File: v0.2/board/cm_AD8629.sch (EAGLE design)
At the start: 36 parts, among them U1 LT8582EDKDPBF

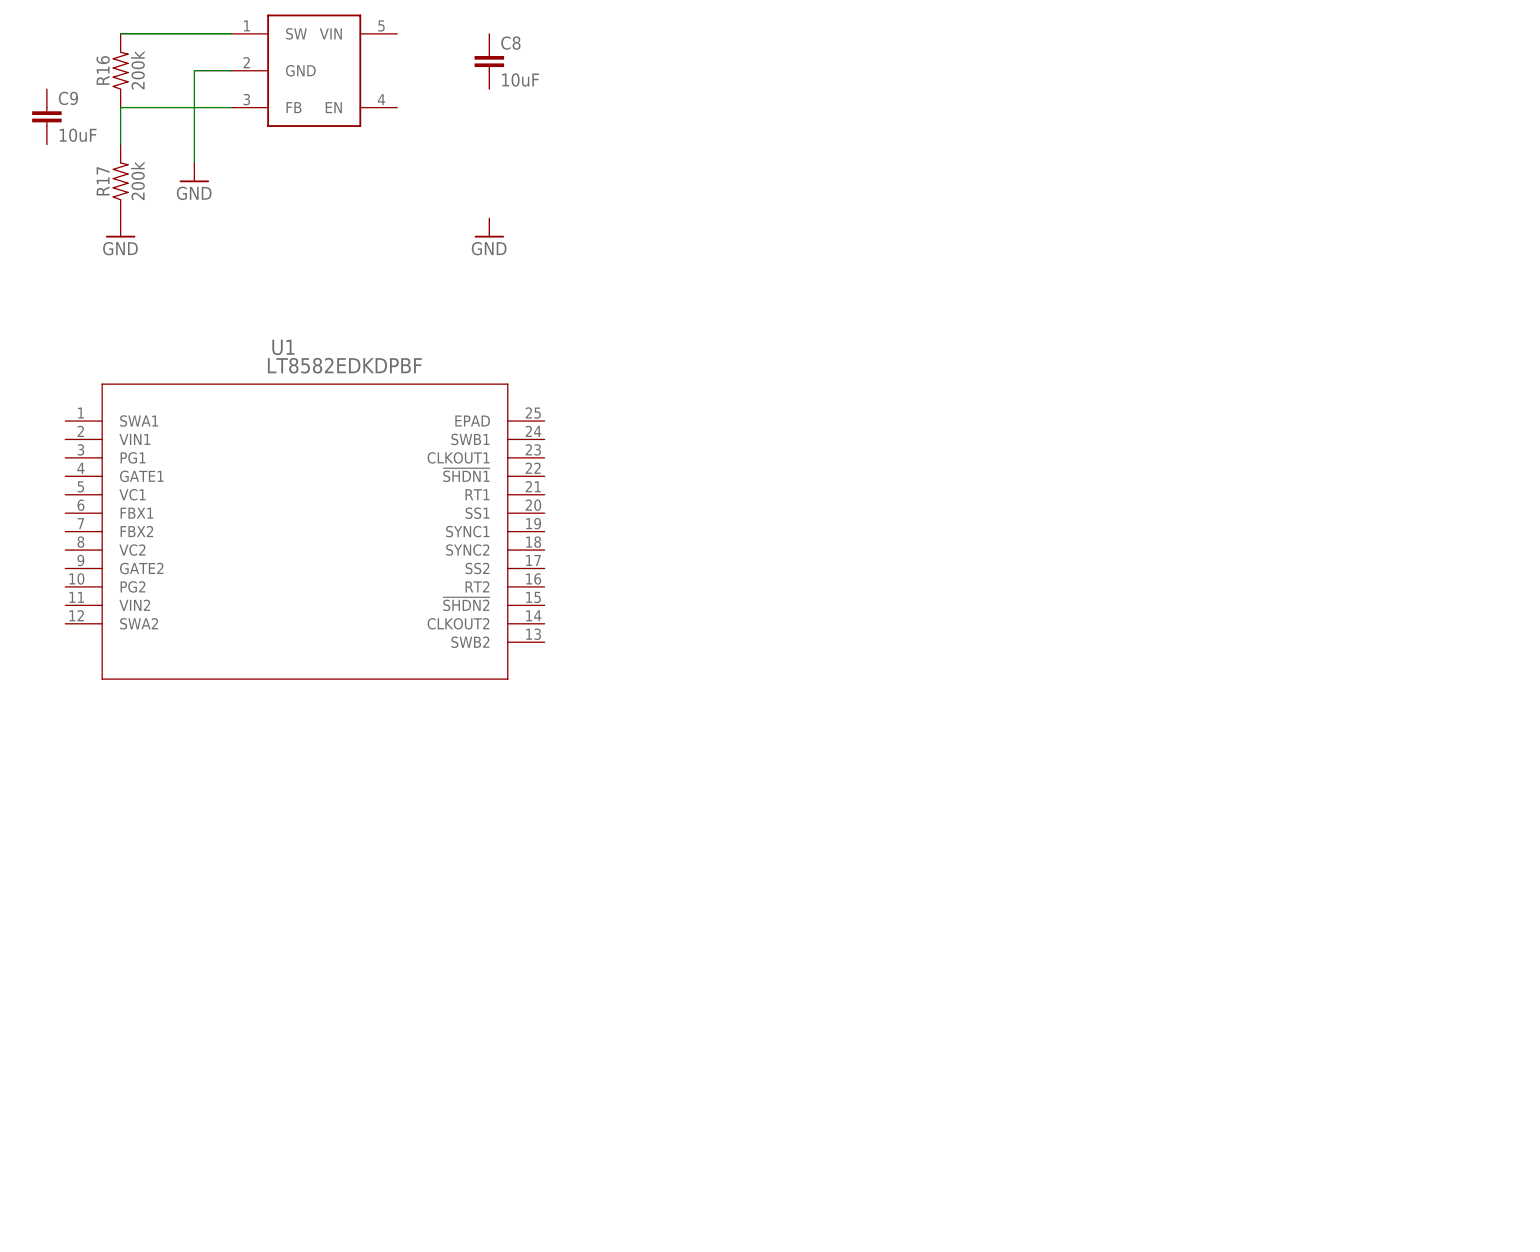
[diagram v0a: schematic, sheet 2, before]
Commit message: add 12v boost to sch
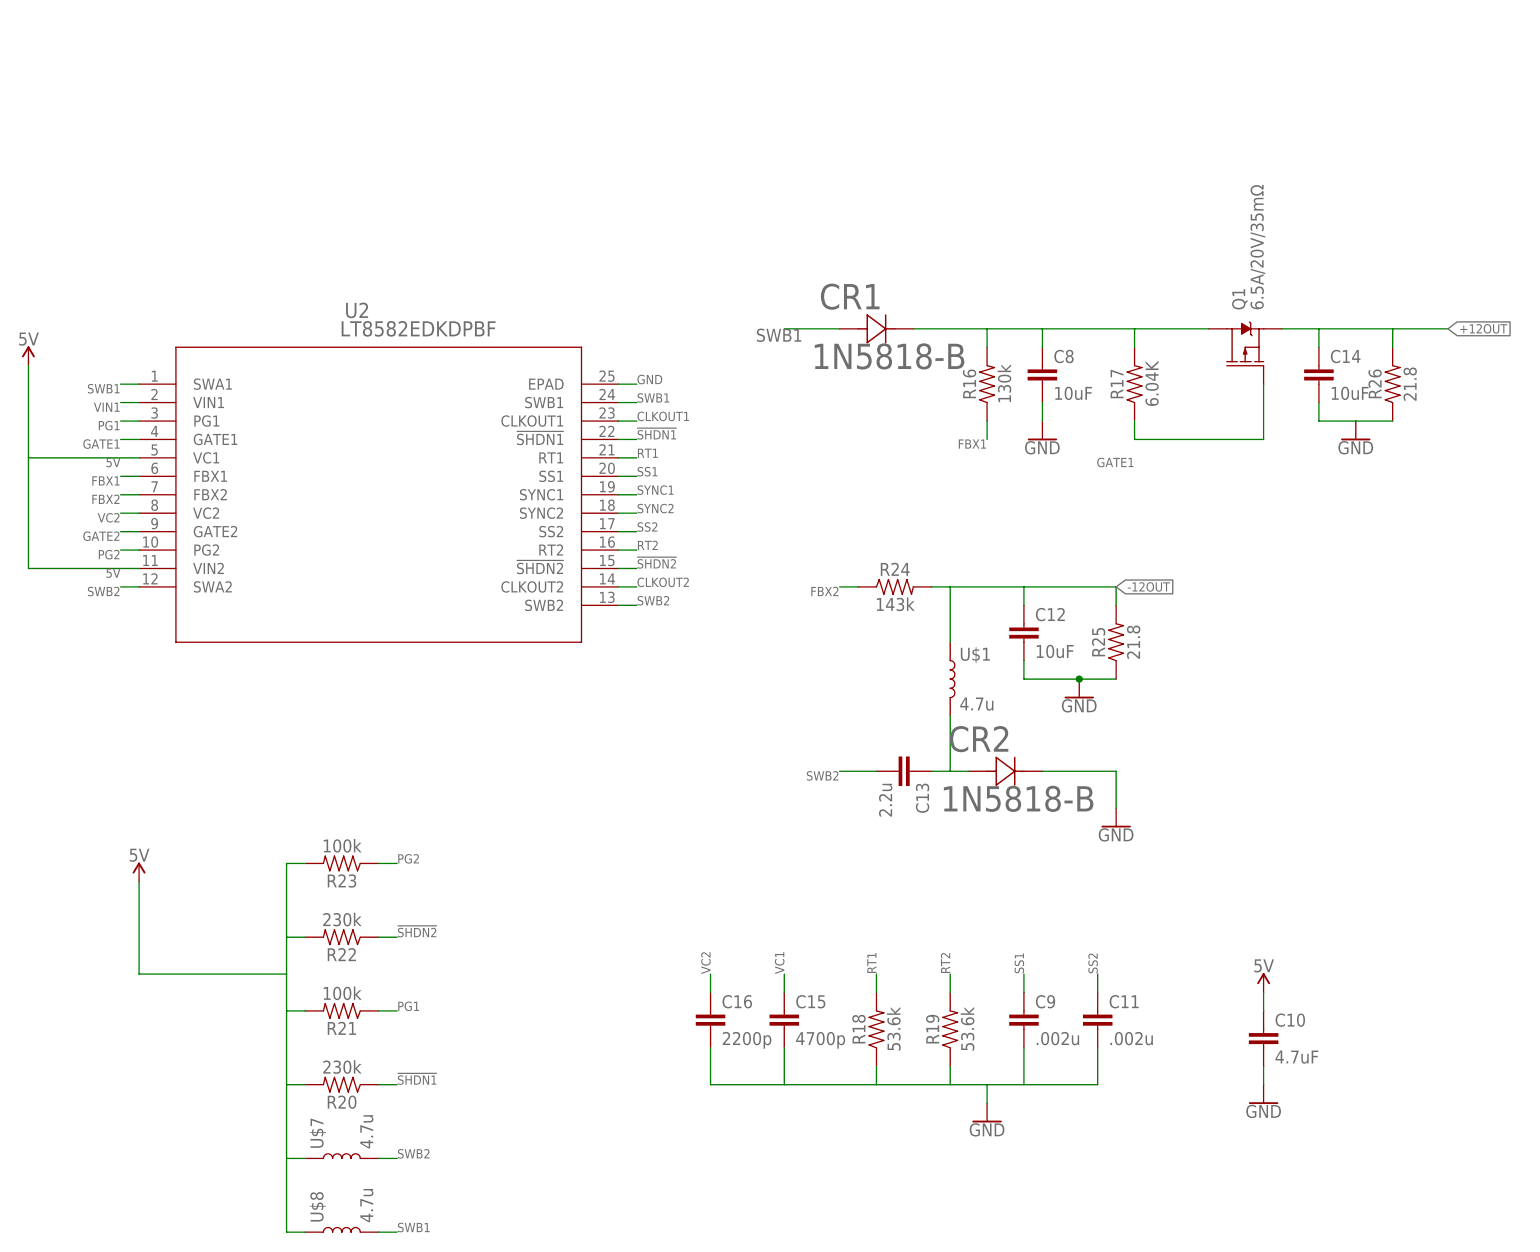
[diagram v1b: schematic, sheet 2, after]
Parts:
- removed U1: LT8582EDKDPBF, Lt8582:LT8582EDKDPBF
- added C10: 4.7uF, SparkFun-Capacitors:10UF-0603-6.3V-20%
- added C11: .002u, SparkFun-Capacitors:10UF-0603-6.3V-20%
- added C12, C14: 10uF, SparkFun-Capacitors:10UF-0603-6.3V-20%
- added C13: 2.2u, SparkFun-Capacitors:10UF-0603-6.3V-20%
- added C15: 4700p, SparkFun-Capacitors:10UF-0603-6.3V-20%
- added C16: 2200p, SparkFun-Capacitors:10UF-0603-6.3V-20%
- added CR1, CR2: 1N5818-B, 1N5818-B:1N5818-B
- added Q1: 6.5A/20V/35mΩ, SparkFun-DiscreteSemi:MOSFET_PCH-NDS8434
- added R18, R19: 53.6k, SparkFun-Resistors:150KOHM-0603-1/10W-1%
- added R20, R22: 230k, SparkFun-Resistors:150KOHM-0603-1/10W-1%
- added R21, R23: 100k, SparkFun-Resistors:150KOHM-0603-1/10W-1%
- added R24: 143k, SparkFun-Resistors:150KOHM-0603-1/10W-1%
- added R25, R26: 21.8, SparkFun-Resistors:150KOHM-0603-1/10W-1%
- added U$7, U$8: 4.7u, SparkFun-Coils:1239AS-H
- added U2: LT8582EDKDPBF, LT8582:LT8582EDKDPBF
- C9: value 10uF -> .002u
- R16: value 200k -> 130k; device SparkFun-Resistors:200KOHM-0603-1/10W-1% -> SparkFun-Resistors:150KOHM-0603-1/10W-1%
- R17: value 200k -> 6.04K; device SparkFun-Resistors:200KOHM-0603-1/10W-1% -> SparkFun-Resistors:150KOHM-0603-1/10W-1%
- U$1: value MIC2250 -> 4.7u; device MIC2250:MIC2250 -> SparkFun-Coils:1239AS-H
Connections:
- net +8V renamed +12V
- net -8V renamed -12V
- removed net N$12: R16.1, R17.2, U$1.FB
- removed net V+: POWER.2, U$6.I1
- new net !SHDN1: R20.1, U2.!SHDN1
- new net !SHDN2: R22.1, U2.!SHDN2
- new net +12OUT: C14.1, Q1.S, R26.2
- new net -12OUT: C12.1, R24.2, R25.2, U$1.1
- new net 5V: C10.1, R20.2, R21.2, R22.2, R23.2, U$7.1, U$8.1, U2.VC1, U2.VIN2
- new net CLKOUT1: U2.CLKOUT1
- new net CLKOUT2: U2.CLKOUT2
- new net FBX1: R16.1, U2.FBX1
- new net FBX2: R24.1, U2.FBX2
- new net GATE1: Q1.G, R17.1, U2.GATE1
- new net GATE2: U2.GATE2
- new net N$14: C13.1, CR2.21, U$1.2
- new net PG1: R21.1, U2.PG1
- new net PG2: R23.1, U2.PG2
- new net RT1: R18.2, U2.RT1
- new net RT2: R19.2, U2.RT2
- new net SS1: C9.1, U2.SS1
- new net SS2: C11.1, U2.SS2
- new net SWB1: CR1.21, U$8.2, U2.SWA1, U2.SWB1
- new net SWB2: C13.2, U$7.2, U2.SWA2, U2.SWB2
- new net SYNC1: U2.SYNC1
- new net SYNC2: U2.SYNC2
- new net VC1: C15.1
- new net VC2: C16.1, U2.VC2
- new net VIN1: U2.VIN1
- new net V_BATT: POWER.2, R1.1, U$5.IN+, U$6.I1
- net GND: now also C10.2, C11.2, C12.2, C14.2, C15.2, C16.2, C8.2, C9.2, CR2.12, R18.1, R19.1, R25.1, R26.1, U2.EPAD; no longer R17.1, U$1.GND
- net N$13: now also C8.1, CR1.12, Q1.D, R17.2; no longer U$1.SW
- net VSS: now also R5.1, U$5.IN-
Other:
- note added: "VDD -> 5.5V Supply"
- note added: "V_BATT -> 5V Supply"
- moved on the sheet: C4, C5, C6, C7, C8, C9, R14, R15, R16, R17, U$6

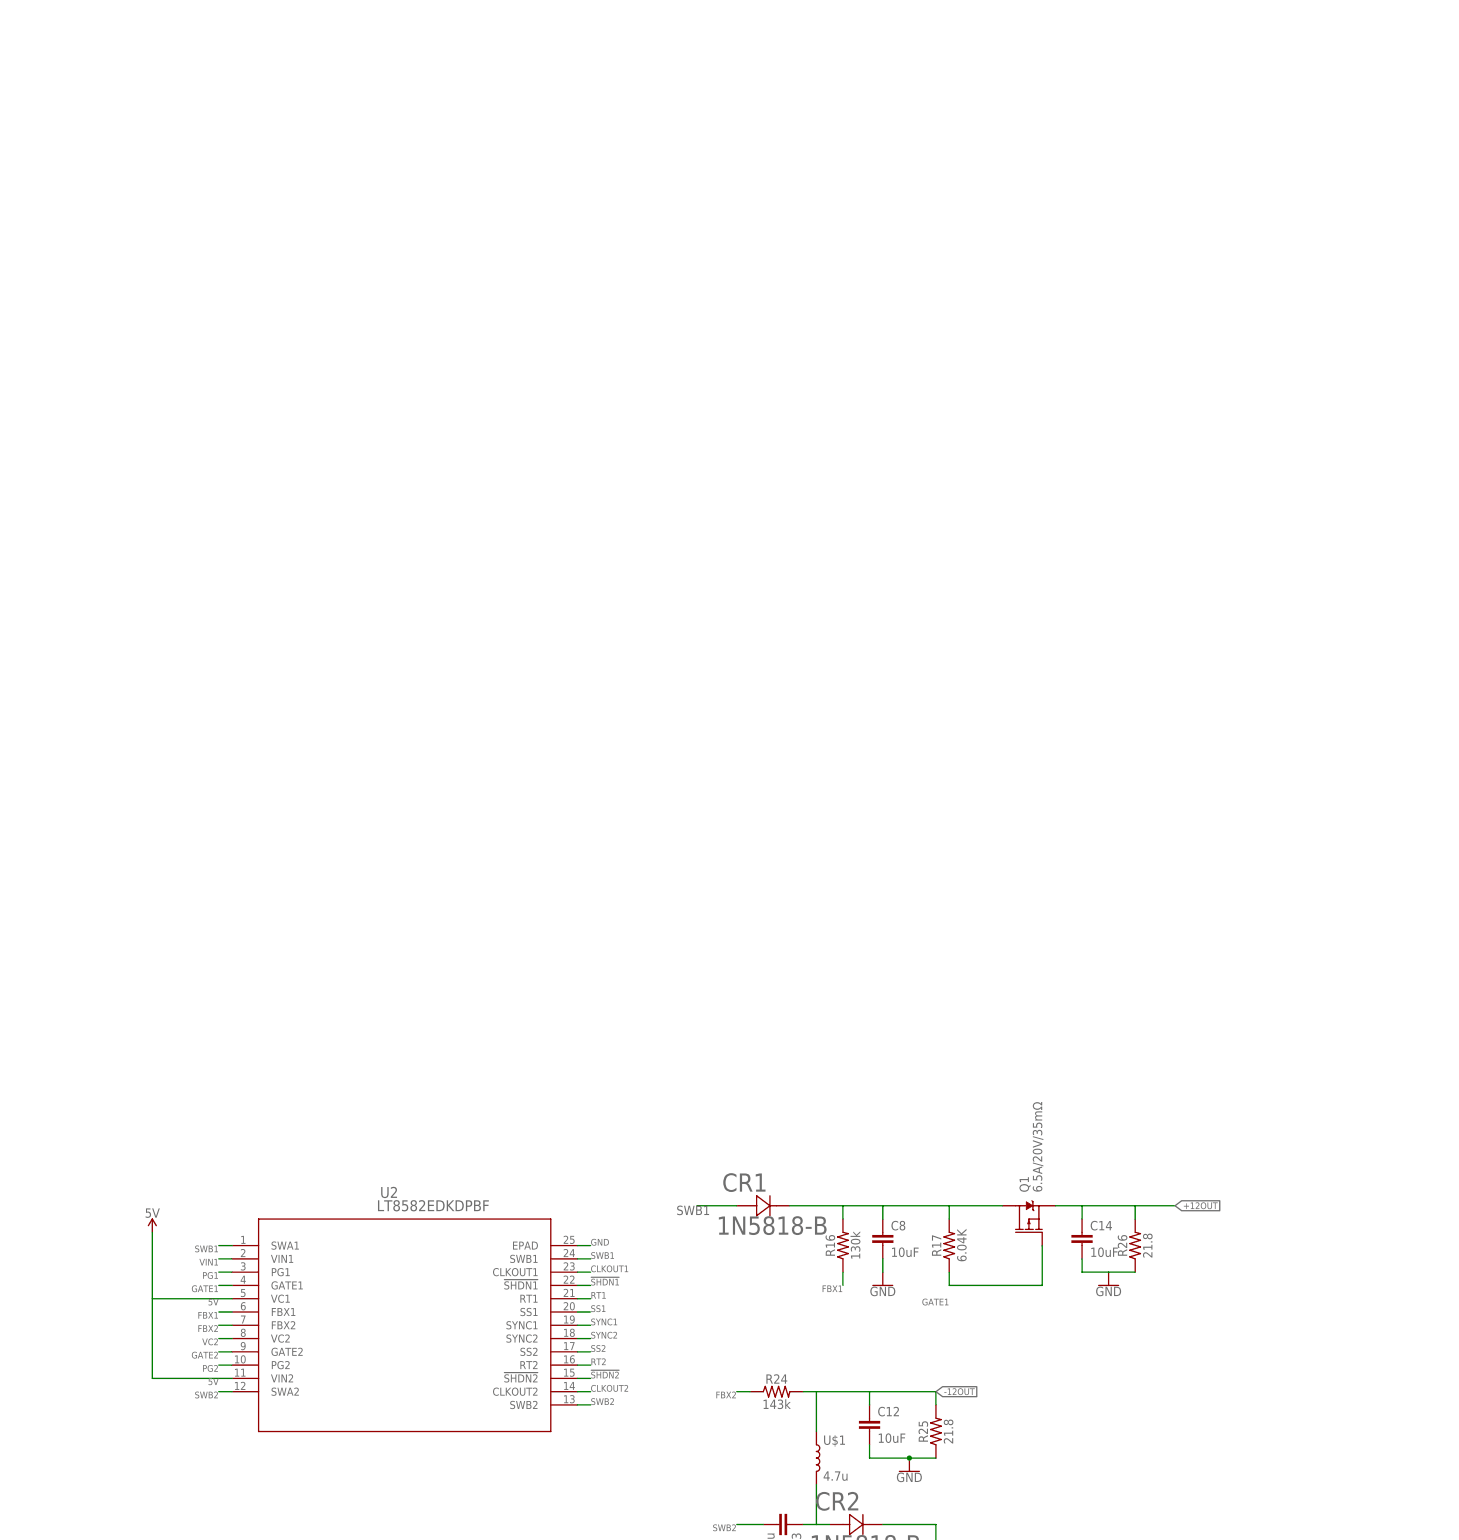
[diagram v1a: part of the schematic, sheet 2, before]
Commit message: add regulator and boost
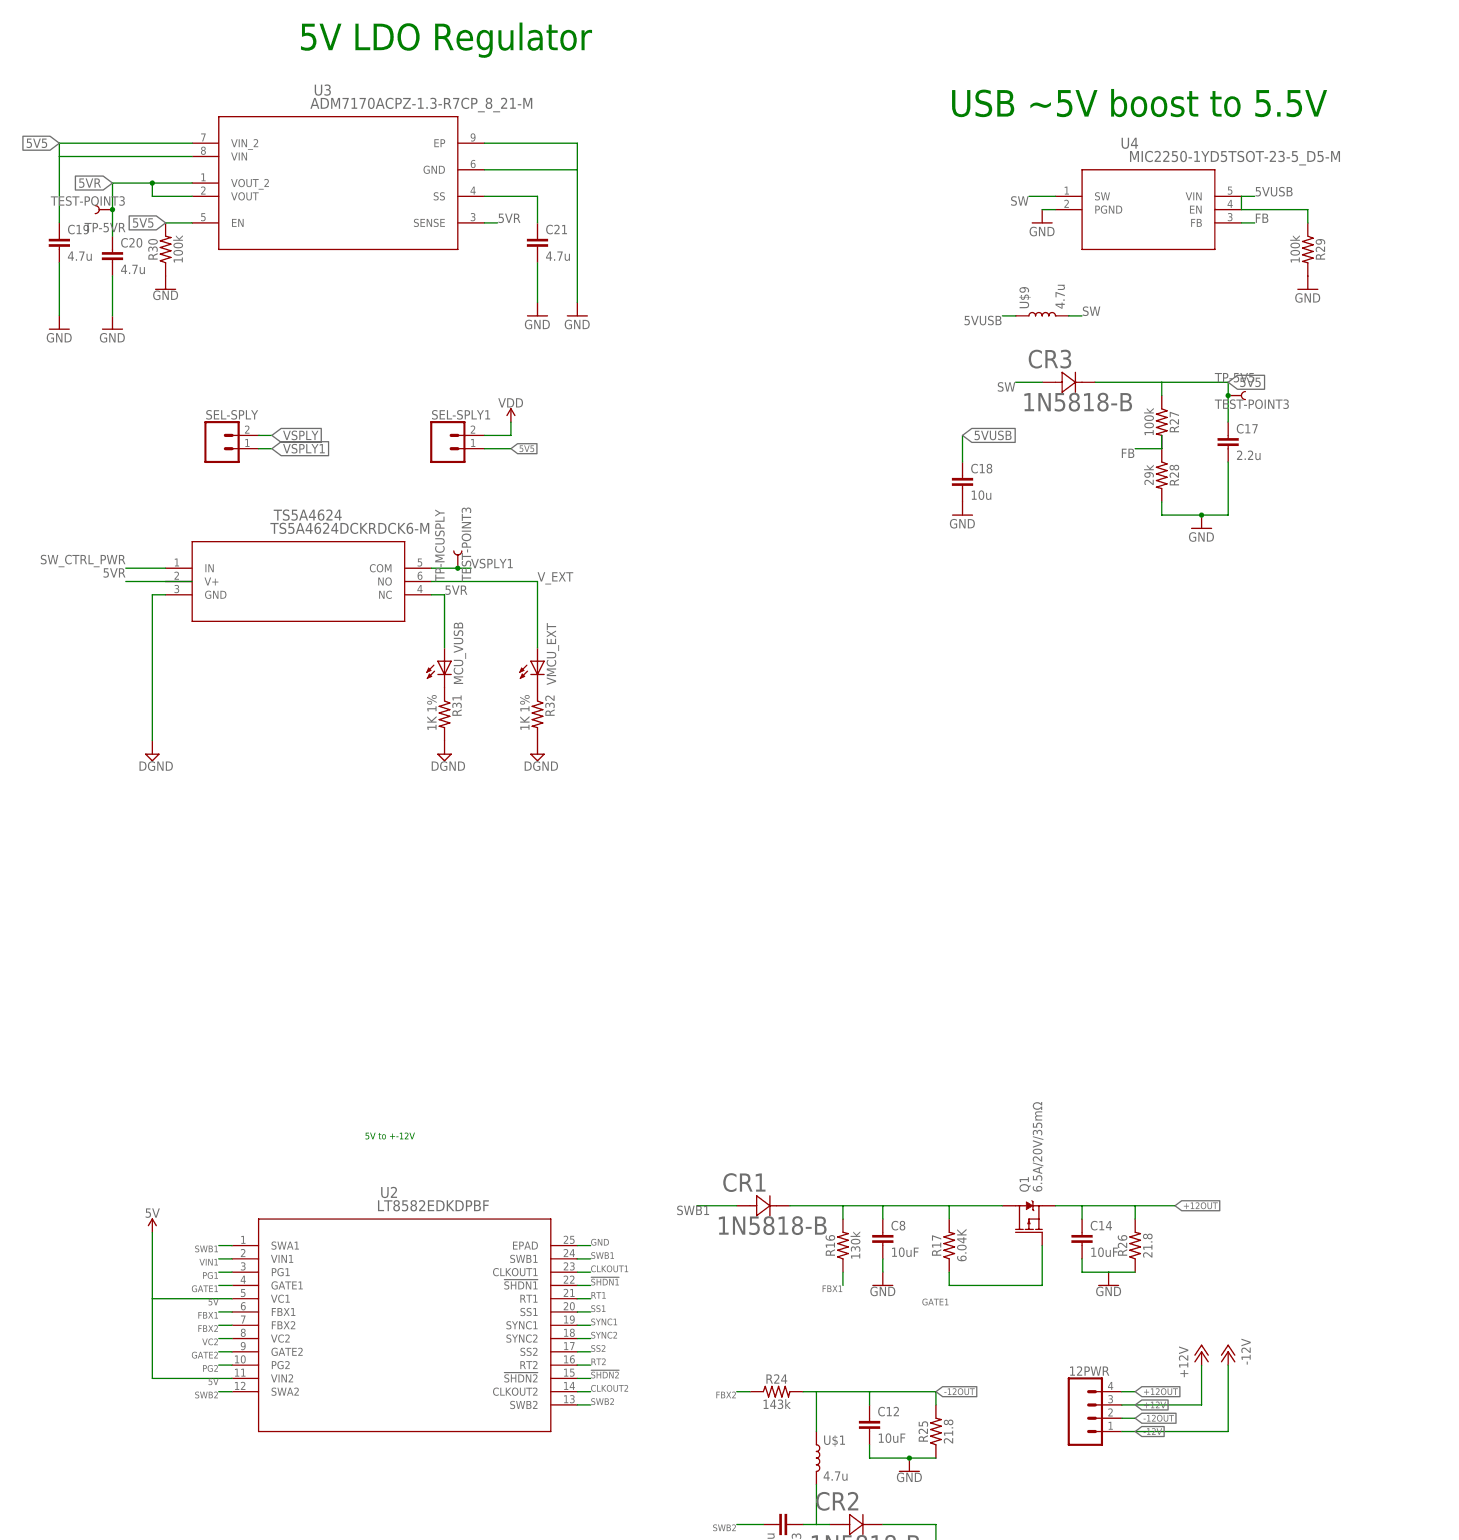
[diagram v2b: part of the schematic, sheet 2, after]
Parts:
- added 12PWR: (no value), SparkFun-Connectors:CONN_04
- added C17: 2.2u, SparkFun-Capacitors:10UF-0603-6.3V-20%
- added C18: 10u, SparkFun-Capacitors:10UF-0603-6.3V-20%
- added C19, C20, C21: 4.7u, SparkFun-Capacitors:10UF-0603-6.3V-20%
- added CR3: 1N5818-B, 1N5818-B:1N5818-B
- added MCU_VUSB, VMCU_EXT: (no value), led:LEDCHIPLED_0603
- added R27, R29, R30: 100k, SparkFun-Resistors:150KOHM-0603-1/10W-1%
- added R28: 29k, SparkFun-Resistors:150KOHM-0603-1/10W-1%
- added R31, R32: 1K 1%, rcl:R-US_R0603
- added SEL-SPLY, SEL-SPLY1: (no value), SparkFun-Connectors:CONN_02
- added TP-5V5, TP-5VR, TP-MCUSPLY: TEST-POINT3, SparkFun-Connectors:TEST-POINT3
- added TS5A4624: TS5A4624DCKRDCK6-M, texas_instruments:TS5A4624DCKRDCK6-M
- added U$9: 4.7u, SparkFun-Coils:1239AS-H
- added U3: ADM7170ACPZ-1.3-R7CP_8_21-M, analog_devices:ADM7170ACPZ-1.3-R7CP_8_21-M
- added U4: MIC2250-1YD5TSOT-23-5_D5-M, texas_instruments:MIC2250-1YD5TSOT-23-5_D5-M
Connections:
- new net 5V5: C17.1, C19.1, CR3.12, R27.1, R30.2, SEL-SPLY1.1, TP-5V5.1, U3.EN, U3.VIN, U3.VIN_2
- new net 5VR: C20.1, MCU_VUSB.A, TP-5VR.1, TS5A4624.NC, TS5A4624.V+, U3.SENSE, U3.VOUT, U3.VOUT_2
- new net 5VUSB: C18.1, R29.1, U$9.1, U4.EN, U4.VIN
- new net DGND: R31.2, R32.2, TS5A4624.GND
- new net FB: R28.1, U4.FB
- new net N$20: C21.1, U3.SS
- new net N$25: MCU_VUSB.C, R31.1
- new net N$26: R32.1, VMCU_EXT.C
- new net SW: CR3.21, U$9.2, U4.SW
- new net SW_CTRL_PWR: TS5A4624.IN
- new net VSPLY: POWER.2, SEL-SPLY.2, U$6.I1
- new net VSPLY1: SEL-SPLY.1, TP-MCUSPLY.1, TS5A4624.COM
- new net V_EXT: TS5A4624.NO, VMCU_EXT.A
- net +12OUT: now also 12PWR.4
- net +12V: now also 12PWR.3
- net -12OUT: now also 12PWR.2
- net -12V: now also 12PWR.1
- net GND: now also C17.2, C18.2, C19.2, C20.2, C21.2, R28.2, R29.2, R30.1, U3.EP, U3.GND, U4.PGND
- net VDD: now also SEL-SPLY1.2
- net V_BATT: no longer POWER.2, U$6.I1
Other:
- note added: "5V LDO Regulator"
- note added: "5V to +-12V"
- note added: "USB ~5V boost to 5.5V"
